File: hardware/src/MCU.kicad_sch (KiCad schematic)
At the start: 19 parts, among them SW201 SW_Push, SW202 SW_Push, U201 ESP32-C3-WROOM-02, U202 TLV1117LV33

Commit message: Add: Brightness sensors to the schematic
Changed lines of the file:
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@@
 		)
 	)
-	(text_box "Can also be replaced with a standard TLV1117, both ICs are pin-compatible"
+	(text_box "Can also be replaced with a weaker standard TLV1117, both ICs are pin-compatible"
 		(exclude_from_sim no)
 		(at 199.39 85.09 0)

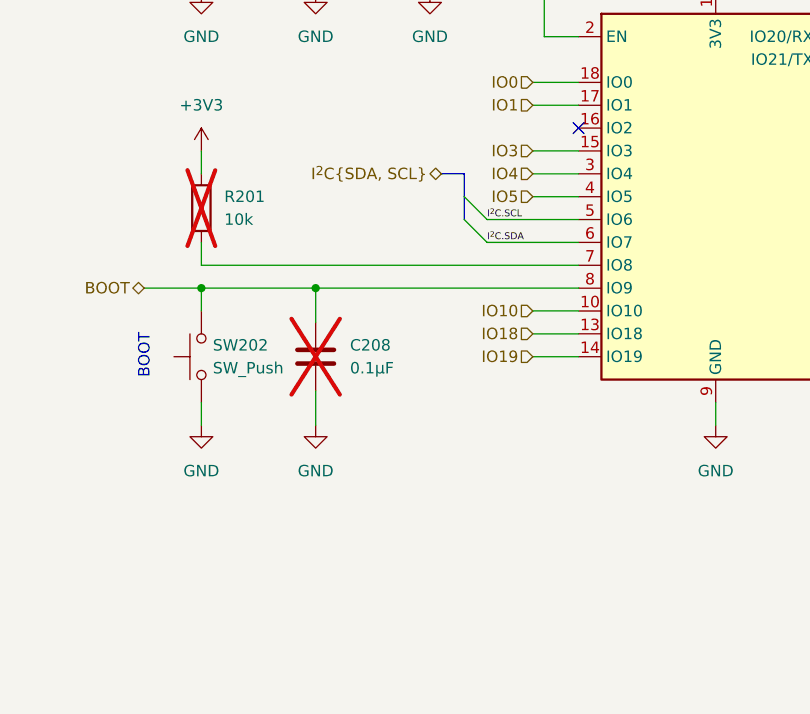
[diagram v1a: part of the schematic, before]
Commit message: Add: Alternative USB connection, directly to the ESP USB_DP and USB_DN
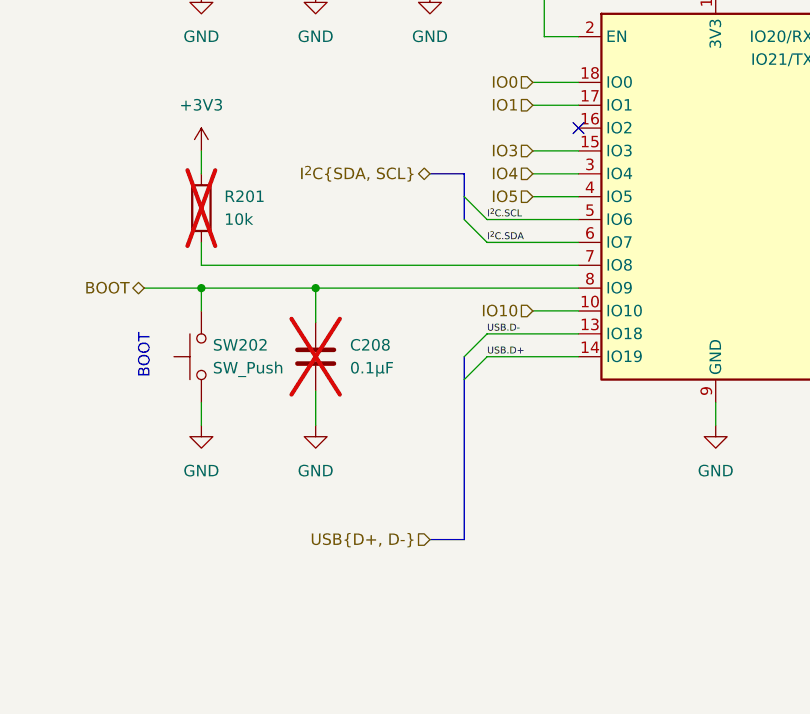
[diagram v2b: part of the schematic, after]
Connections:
- net IO18 renamed USB.D-
- net IO19 renamed USB.D+
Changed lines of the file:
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@@
+		)
+	)
+	(bus_entry
+		(at 80.01 119.38)
+		(size 2.54 -2.54)
+		(stroke
+			(width 0)
+			(type default)
+		)
+	)
+	(bus_entry
+		(at 80.01 121.92)
+		(size 2.54 -2.54)
+		(stroke
+			(width 0)
+			(type default)
 		)
 	)
@@
 	(wire
 		(pts
+			(xy 82.55 119.38) (xy 92.71 119.38)
+		)
+		(stroke
+			(width 0)
+			(type default)
+		)
+	)
+	(wire
+		(pts
 			(xy 63.5 63.5) (xy 76.2 63.5)
 		)
@@
 	(wire
 		(pts
+			(xy 82.55 116.84) (xy 92.71 116.84)
+		)
+		(stroke
+			(width 0)
+			(type default)
+		)
+	)
+	(wire
+		(pts
 			(xy 76.2 67.31) (xy 76.2 63.5)
 		)
@@
 	(wire
 		(pts
-			(xy 87.63 119.38) (xy 92.71 119.38)
-		)
-		(stroke
-			(width 0)
-			(type default)
-		)
-	)
-	(wire
-		(pts
 			(xy 107.95 76.2) (xy 107.95 78.74)
 		)
@@
 		)
 	)
+	(bus
+		(pts
+			(xy 80.01 139.7) (xy 76.2 139.7)
+		)
+		(stroke
+			(width 0)
+			(type default)
+		)
+	)
 	(wire
 		(pts
@@
 	(bus
 		(pts
-			(xy 80.01 99.06) (xy 77.47 99.06)
+			(xy 80.01 99.06) (xy 76.2 99.06)
 		)
 		(stroke
@@
 		)
 	)
+	(bus
+		(pts
+			(xy 80.01 119.38) (xy 80.01 121.92)
+		)
+		(stroke
+			(width 0)
+			(type default)
+		)
+	)
 	(wire
 		(pts
@@
 		)
 	)
+	(bus
+		(pts
+			(xy 80.01 121.92) (xy 80.01 139.7)
+		)
+		(stroke
+			(width 0)
+			(type default)
+		)
+	)
 	(wire
 		(pts
@@
 		(pts
 			(xy 135.89 83.82) (xy 135.89 81.28)
-		)
-		(stroke
-			(width 0)
-			(type default)
-		)
-	)
-	(wire
-		(pts
-			(xy 87.63 116.84) (xy 92.71 116.84)
 		)
 		(stroke
@@
 		)
 	)
+	(label "USB.D-"
+		(at 82.55 116.84 0)
+		(fields_autoplaced yes)
+		(effects
+			(font
+				(size 0.762 0.762)
+			)
+			(justify left bottom)
+		)
+	)
 	(label "I^{2}C.SDA"
 		(at 82.55 106.68 0)
+		(fields_autoplaced yes)
+		(effects
+			(font
+				(size 0.762 0.762)
+			)
+			(justify left bottom)
+		)
+	)
+	(label "USB.D+"
+		(at 82.55 119.38 0)
 		(fields_autoplaced yes)
 		(effects
@@
 		)
 	)
+	(hierarchical_label "USB{D+, D-}"
+		(shape input)
+		(at 76.2 139.7 180)
+		(fields_autoplaced yes)
+		(effects
+			(font
+				(size 1.27 1.27)
+			)
+			(justify right)
+		)
+	)
 	(hierarchical_label "~{RST}"
 		(shape bidirectional)
@@
 		)
 	)
-	(hierarchical_label "IO18"
-		(shape input)
-		(at 87.63 116.84 180)
-		(fields_autoplaced yes)
-		(effects
-			(font
-				(size 1.27 1.27)
-			)
-			(justify right)
-		)
-	)
 	(hierarchical_label "IO1"
 		(shape input)
@@
 		)
 	)
-	(hierarchical_label "IO19"
-		(shape input)
-		(at 87.63 119.38 180)
-		(fields_autoplaced yes)
-		(effects
-			(font
-				(size 1.27 1.27)
-			)
-			(justify right)
-		)
-	)
 	(hierarchical_label "IO0"
 		(shape input)
@@
 	(hierarchical_label "I^{2}C{SDA, SCL}"
 		(shape bidirectional)
-		(at 77.47 99.06 180)
-		(fields_autoplaced yes)
-		(effects
+		(at 76.2 99.06 180)
+		(fields_autoplaced yes)
+		(effects
